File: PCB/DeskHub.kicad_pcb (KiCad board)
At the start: 4 copper layers, 212.6 x 134.5 mm, 120 parts, among them J1 USB_A, J2 5V Barrel, J4 USB_A, J5 USB_A, J6 USB_A, J7 USB_A, U1 TUSB4041I, U2 3.3V Reg, U3 1.1V Reg, U4 TPS2001CDGNR, U5 TPS2001CDGNR, U6 TPS2001CDGNR, U7 TPS2001CDGNR, Y1 ECS-240-20-30B-TR

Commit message: routing done!
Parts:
- C16, C17, FB6, R6: moved to B.Cu
- moved C27 186.0 mm to (168.3, 87.5), turned to -90 degrees
- moved C22 152.3 mm to (133.9, 79.6), turned to 90 degrees
- moved FB6 108.0 mm to (169.8, 83.3)
- moved R23 72.1 mm to (173.4, 99.0)
- moved R24 68.9 mm to (173.4, 97.5)
- moved R25 65.7 mm to (173.4, 96.0)
- moved R26 62.6 mm to (173.4, 94.5)
- moved R27 59.5 mm to (173.4, 93.0), turned to 180 degrees
- moved R15 58.0 mm to (165.5, 91.8)
- moved R21 55.3 mm to (165.5, 92.8)
- moved R20 55.1 mm to (165.6, 90.6)
- moved R22 54.4 mm to (165.5, 93.8)
- moved R1 51.5 mm to (128.7, 82.5), turned to 180 degrees
- moved R6 51.4 mm to (89.3, 33.6), turned to -90 degrees
- moved R3 44.6 mm to (151.8, 79.3)
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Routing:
- net /Port 1 Power Switch/PWRON_EN: track 1.93 -> 142.0 mm, vias 1 -> 2
- net /Port 4 Power Switch/PWRON_EN: track 0.00 -> 130.1 mm, vias 0 -> 2
- net /Port 1 Power Switch/OVERCURRENT: track 3.85 -> 125.0 mm, vias 1 -> 2
- net /Port 4 Power Switch/OVERCURRENT: track 3.29 -> 120.6 mm, vias 1 -> 2
- net USB_UP_D-: track 0.00 -> 100.9 mm
- net USB_UP_D+: track 0.00 -> 100.9 mm
- net /Port 2 Power Switch/PWRON_EN: track 1.74 -> 98.1 mm, vias 1 -> 2
- net /Port 3 Power Switch/PWRON_EN: track 0.00 -> 91.3 mm, vias 0 -> 2
- net USB_5V_UP: track 0.00 -> 87.7 mm
- net /Port 2 Power Switch/OVERCURRENT: track 4.14 -> 84.4 mm, vias 1 -> 2
- net /Port 3 Power Switch/OVERCURRENT: track 3.18 -> 80.3 mm, vias 1 -> 2
- net Net-(U1-PWRCTL_POL): track 0.00 -> 24.1 mm, vias 0 -> 2
- net Net-(U1-TEST): track 0.00 -> 19.1 mm
- net Net-(U1-USB_VBUS): track 0.00 -> 17.2 mm, vias 0 -> 2
- net Net-(U1-FULLPWRMGMTz/SMBA1): track 0.00 -> 16.6 mm
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- added copper zone on B.Cu, net VDD3.3
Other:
- board text removed: "1.1"
- board text removed: "3.3"

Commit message: finished v1 of board
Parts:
- moved C20 4.62 mm to (134.9, 96.6), turned to 180 degrees
- moved C4 3.91 mm to (134.4, 97.3), turned to 180 degrees
- moved C18 3.76 mm to (146.8, 85.6), turned to 90 degrees
- moved C2 3.32 mm to (147.5, 85.0), turned to 90 degrees
- moved C25 2.43 mm to (134.9, 98.0), turned to 180 degrees
- moved C19 2.13 mm to (139.3, 87.3), turned to -90 degrees
- moved C26 2.00 mm to (149.2, 96.2), turned to 180 degrees
- moved C24 1.97 mm to (140.8, 87.4), turned to -90 degrees
- moved C23 1.95 mm to (148.2, 85.5), turned to 90 degrees
- moved C3 1.68 mm to (140.1, 87.8), turned to -90 degrees
- moved C21 1.66 mm to (149.2, 97.7), turned to 180 degrees
- moved C5 1.45 mm to (148.8, 97.0), turned to 180 degrees
- moved C63 0.30 mm to (142.3, 159.2), turned to 90 degrees
- moved R16 0.15 mm to (140.1, 159.2)
- moved C64 0.10 mm to (141.2, 159.2)
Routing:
- net BOARD_3.3V: track 12.4 -> 4.69 mm, vias 46 -> 42
- net VDD3.3: track 21.2 -> 16.0 mm
- net Earth: track 27.2 -> 28.0 mm, vias 65 -> 51
- net BOARD_1.1V: vias 12 -> 4
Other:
- board size 212.6 x 134.5 mm -> 212.6 x 139.5 mm

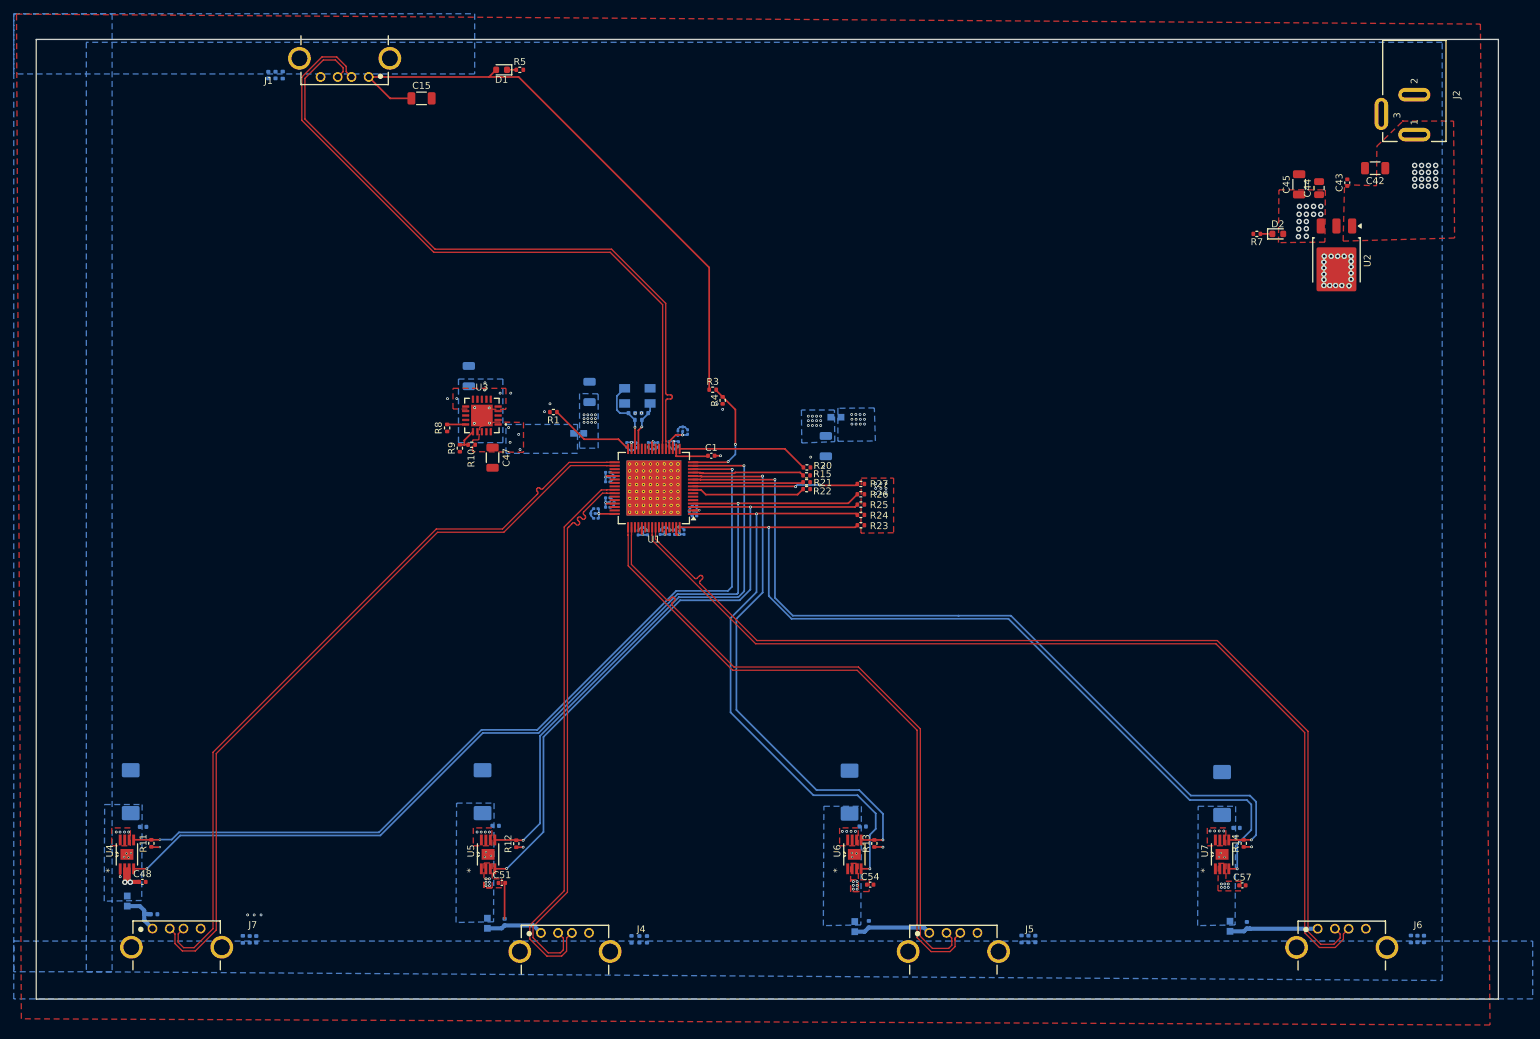
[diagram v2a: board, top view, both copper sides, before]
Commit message: pcb v1.1, modified to conform to JLC standards
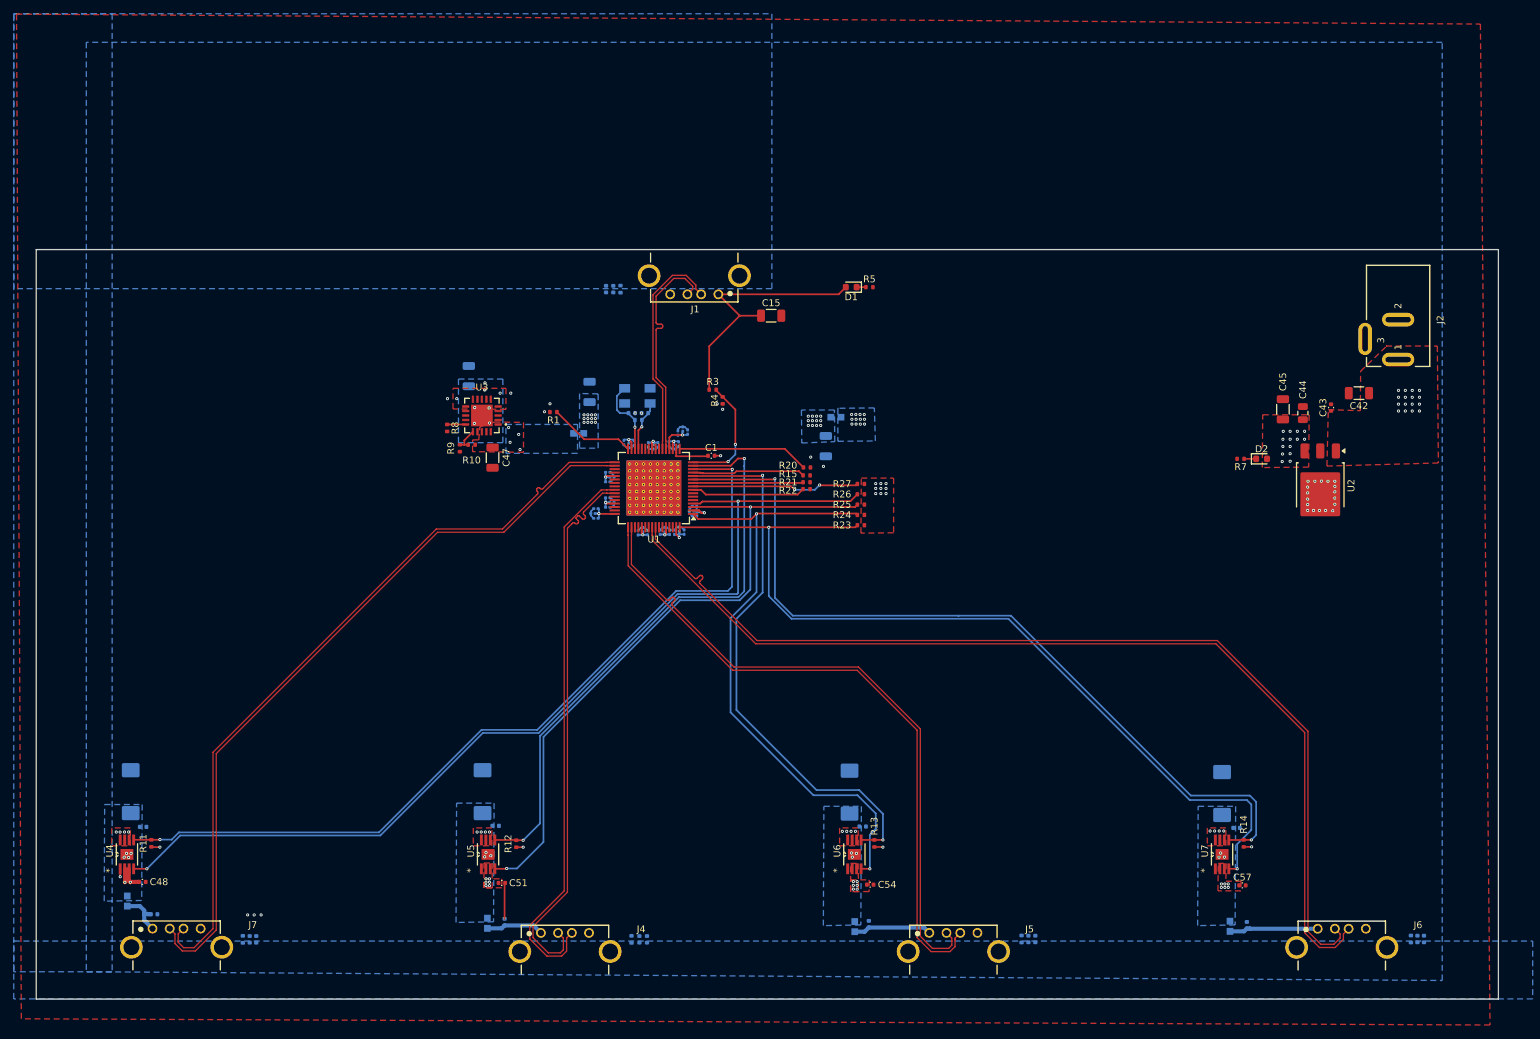
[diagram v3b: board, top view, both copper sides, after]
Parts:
- C1, C13, C14, C16, C17, C43, C48, C49, C51, C52, C54, C55, C57, C58, C63, C64, C65, C66, C67, C68, C69, C70, C71, C72, C73, C74: footprint Capacitor_SMD:C_0402_1005Metric -> my_global:C_0402_1005Metric_1.5mm_silkscreen_clearance
- R1, R10, R11, R12, R13, R14, R15, R16, R17, R18, R19, R2, R20, R21, R22, R23, R24, R25, R26, R27, R3, R4, R5, R6, R7, R8, R9: footprint Resistor_SMD:R_0402_1005Metric -> my_global:R_0402_1005Metric_1.5mm_silkscreen_clearance
- moved D1 59.8 mm to (172.0, 64.4)
- moved J1 59.8 mm to (149.2, 59.4)
- moved C15 59.8 mm to (160.3, 68.5)
- moved R5 59.8 mm to (174.6, 64.4)
- moved C17 58.1 mm to (137.4, 64.7)
- moved C16 58.1 mm to (136.3, 64.7)
- moved R6 58.1 mm to (138.4, 64.7)
- moved C43 32.8 mm to (241.7, 81.9)
- moved C44 32.8 mm to (237.6, 82.7)
- moved C45 32.8 mm to (234.7, 82.2)
- moved C42 32.8 mm to (245.8, 79.8)
- moved D2 32.8 mm to (231.6, 89.3)
- moved J2 32.8 mm to (251.5, 69.1)
- moved R7 32.8 mm to (228.6, 89.3)
- moved U2 32.8 mm to (240.2, 93.2)
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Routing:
- net USB_UP_D+: track 100.9 -> 32.6 mm
- net USB_UP_D-: track 100.9 -> 32.6 mm
- net USB_5V_UP: track 87.7 -> 39.0 mm
- net VDD3.3: track 16.0 -> 18.5 mm
- net /Port 2 Power Switch/OVERCURRENT: track 84.4 -> 85.9 mm
- net /Port 2 Power Switch/PWRON_EN: track 98.1 -> 98.9 mm
- net /Port 3 Power Switch/PWRON_EN: track 91.3 -> 91.9 mm
- net VDD1.1: track 22.5 -> 23.1 mm
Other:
- board size 212.6 x 139.5 mm -> 212.6 x 108.9 mm

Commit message: pcb v1.2 with JLC mappings
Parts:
- C50, C53, C56, C59: footprint Capacitor_Tantalum_SMD:CP_EIA-7343-15_Kemet-W -> my_global:CAP_EEFCX0J151XR
- moved C59 0.80 mm to (225.9, 137.2)
- moved C56 0.60 mm to (171.8, 137.2)
- moved J4 0.60 mm to (130.4, 163.7)
- moved J5 0.60 mm to (186.8, 163.7)
- moved C50 0.53 mm to (67.2, 137.2)
- moved C53 0.53 mm to (118.4, 137.2)
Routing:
- net /Port 4 Power Switch/OVERCURRENT: track 120.7 -> 121.4 mm
- net USB_DN2_D-: track 81.1 -> 81.8 mm
- net USB_DN2_D+: track 81.2 -> 81.8 mm
- net /Port 4 Power Switch/PWRON_EN: track 130.1 -> 130.6 mm
- net Earth: vias 51 -> 53
